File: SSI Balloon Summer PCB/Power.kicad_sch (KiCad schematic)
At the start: 37 parts, among them J1 Battery connector, J2 Raspberry Pi Connector, Q2 DMG2305UX-7, SW1 SW_SPDT, U2 TPS63070RNMR, U3 AP2112K-3.3TRG1, U6 TPS63070RNMR

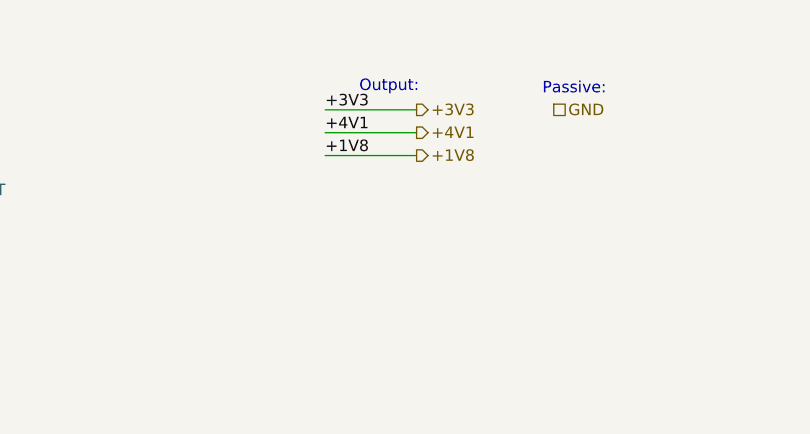
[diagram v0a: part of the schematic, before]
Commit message: Finished sensors + tidied up schematic
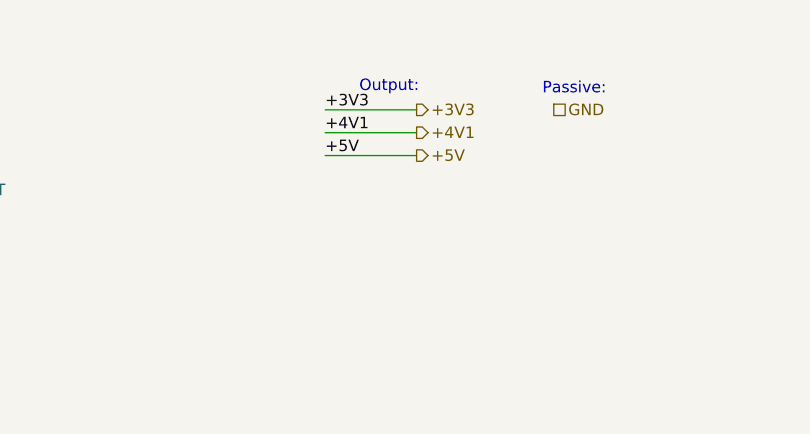
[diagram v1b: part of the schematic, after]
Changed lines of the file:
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@@
+	(wire
+		(pts
+			(xy 226.06 35.56) (xy 236.22 35.56)
+		)
+		(stroke
+			(width 0)
+			(type default)
+		)
+	)
 	(wire
 		(pts
@@
 		(pts
 			(xy 114.3 168.91) (xy 114.3 171.45)
-		)
-		(stroke
-			(width 0)
-			(type default)
-		)
-	)
-	(wire
-		(pts
-			(xy 226.06 35.56) (xy 236.22 35.56)
 		)
 		(stroke
@@
 		)
 	)
-	(label "+1V8"
+	(label "+5V"
 		(at 226.06 35.56 0)
 		(effects
@@
 		)
 	)
-	(hierarchical_label "+1V8"
+	(hierarchical_label "+5V"
 		(shape output)
 		(at 236.22 35.56 0)

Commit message: tidying
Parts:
- removed J2: Raspberry Pi Connector, symbol Connector_Generic:Conn_01x02
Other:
- moved on the sheet: C10, C9, U3

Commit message: Minor tweaks, renamed some pins
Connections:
- no-connect marks 0 -> 1
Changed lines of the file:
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@@
 	)
 	(junction
-		(at 97.79 46.99)
+		(at 82.55 46.99)
 		(diameter 0)
 		(color 0 0 0 0)
@@
 	)
 	(junction
+		(at 97.79 46.99)
+		(diameter 0)
+		(color 0 0 0 0)
+	)
+	(junction
 		(at 267.97 119.38)
 		(diameter 0)
@@
 		(color 0 0 0 0)
 	)
+	(no_connect
+		(at 134.62 50.8)
+	)
 	(wire
 		(pts
@@
 	(wire
 		(pts
-			(xy 92.71 46.99) (xy 97.79 46.99)
+			(xy 82.55 46.99) (xy 97.79 46.99)
 		)
 		(stroke
@@
 	(symbol
 		(lib_id "power:VAA")
-		(at 92.71 46.99 0)
+		(at 82.55 46.99 0)
 		(unit 1)
 		(body_style 1)
@@
 		(fields_autoplaced yes)
 		(property "Reference" "#PWR062"
-			(at 92.71 50.8 0)
+			(at 82.55 50.8 0)
 			(hide yes)
 			(show_name no)
@@
 		)
 		(property "Value" "VBAT"
-			(at 92.71 41.91 0)
+			(at 82.55 41.91 0)
 			(show_name no)
 			(do_not_autoplace no)
@@
 		)
 		(property "Footprint" ""
-			(at 92.71 46.99 0)
+			(at 82.55 46.99 0)
 			(hide yes)
 			(show_name no)
@@
 		)
 		(property "Datasheet" ""
-			(at 92.71 46.99 0)
+			(at 82.55 46.99 0)
 			(hide yes)
 			(show_name no)
@@
 		)
 		(property "Description" "Power symbol creates a global label with name \"VBAT\""
-			(at 92.71 46.99 0)
+			(at 82.55 46.99 0)
 			(hide yes)
 			(show_name no)
@@
 					(unit 1)
 				)
+			)
+		)
+	)
+	(symbol
+		(lib_id "power:PWR_FLAG")
+		(at 82.55 46.99 180)
+		(unit 1)
+		(body_style 1)
+		(exclude_from_sim no)
+		(in_bom yes)
+		(on_board yes)
+		(in_pos_files yes)
+		(dnp no)
+		(fields_autoplaced yes)
+		(property "Reference" "#FLG01"
+			(at 82.55 48.895 0)
+			(hide yes)
+			(show_name no)
+			(do_not_autoplace no)
+			(effects
+				(font
+					(size 1.27 1.27)
+				)
+			)
+		)
+		(property "Value" "PWR_FLAG"
+			(at 82.55 52.07 0)
+			(show_name no)
+			(do_not_autoplace no)
+			(effects
+				(font
+					(size 1.27 1.27)
+				)
+			)
+		)
+		(property "Footprint" ""
+			(at 82.55 46.99 0)
+			(hide yes)
+			(show_name no)
+			(do_not_autoplace no)
+			(effects
+				(font
+					(size 1.27 1.27)
+				)
+			)
+		)
+		(property "Datasheet" ""
+			(at 82.55 46.99 0)
+			(hide yes)
+			(show_name no)
+			(do_not_autoplace no)
+			(effects
+				(font
+					(size 1.27 1.27)
+				)
+			)
+		)
+		(property "Description" "Special symbol for telling ERC where power comes from"
+			(at 82.55 46.99 0)
+			(hide yes)
+			(show_name no)
+			(do_not_autoplace no)
+			(effects
+				(font
+					(size 1.27 1.27)
+				)
+			)
+		)
+		(pin "1"
+		)
+		(instances
+			(project "SSI Summer Balloons"
+				(path "/3c45a535-6e6b-4825-ad52-82c10cbe7866/1b5737e2-4399-496a-b942-ad94430e2078"
+					(reference "#FLG01")
+					(unit 1)
+				)

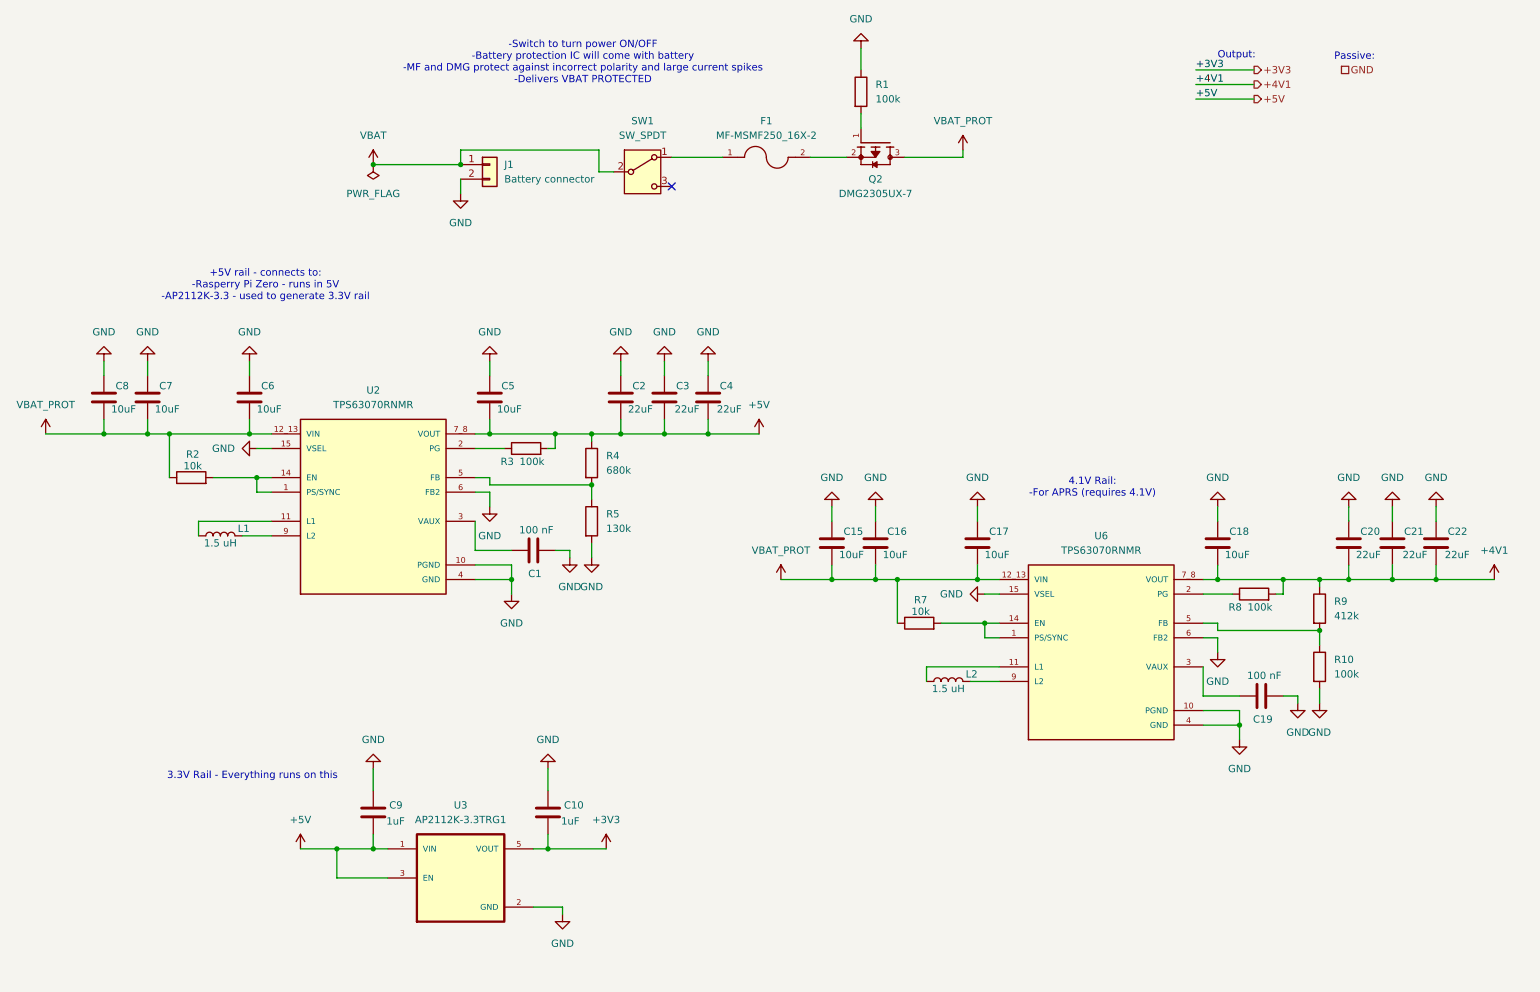
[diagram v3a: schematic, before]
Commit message: Fixed ERC - no ERC errors
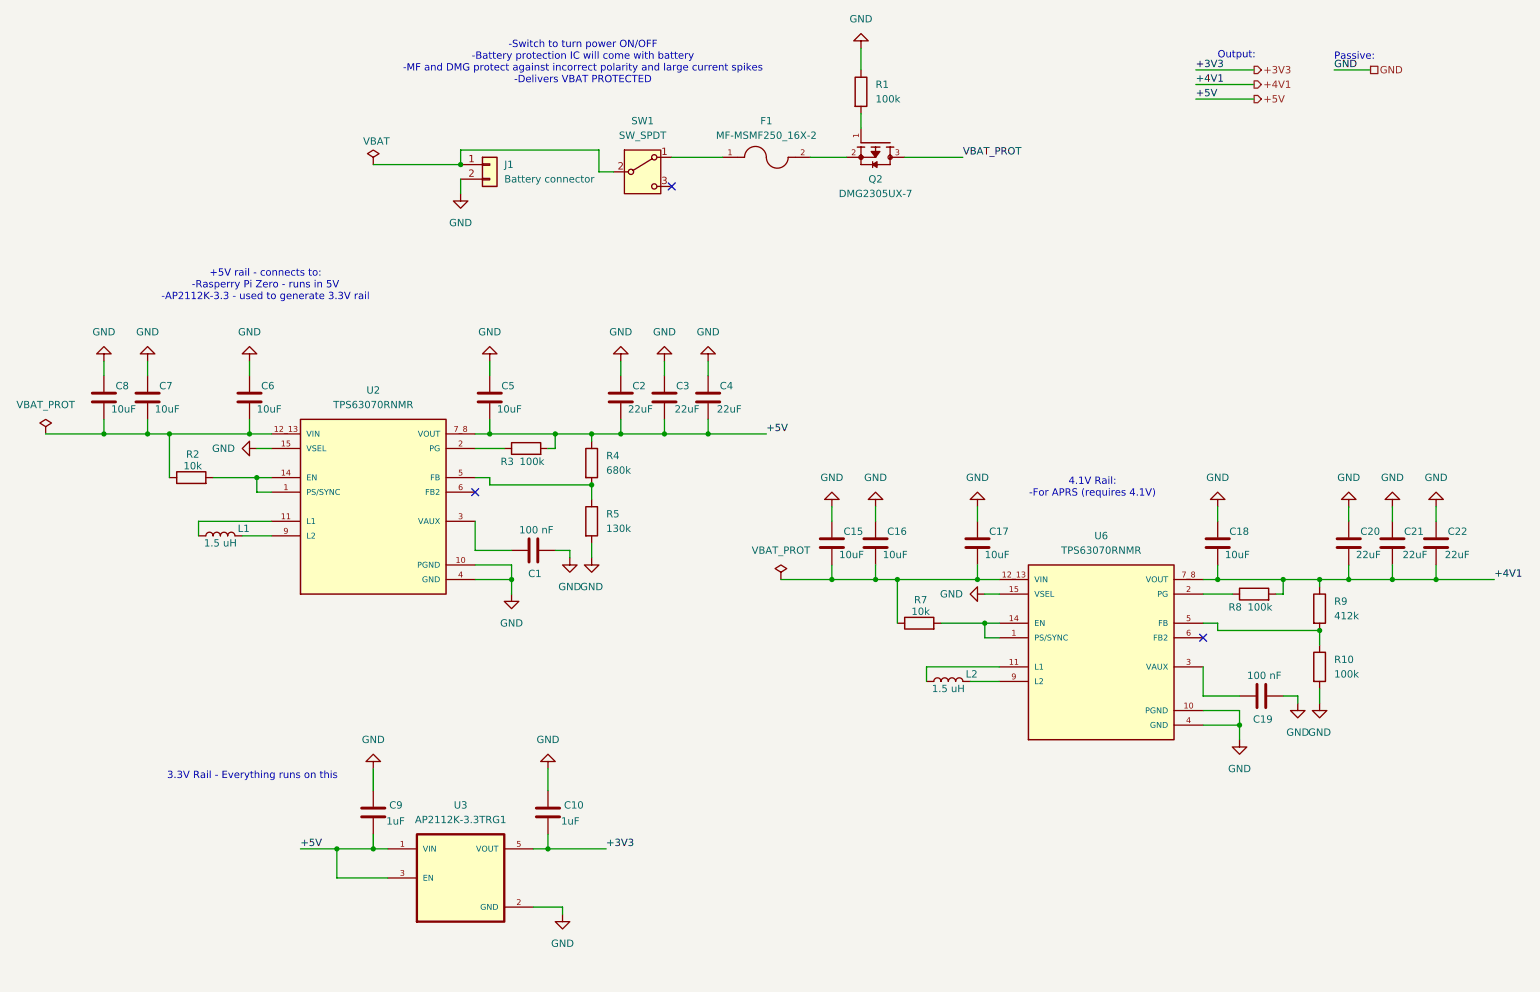
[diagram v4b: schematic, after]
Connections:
- net GND: no longer U2.6 (FB2), U6.6 (FB2)
- net VBAT_PROT: no longer C15.2, C16.2, C17.2, C6.2, C7.2, C8.2, R2.1, R7.1, U2.12_13 (VIN), U6.12_13 (VIN)
- net VBAT: no longer names the net of J1.1 (Pin_1), SW1.2 (B)
- new net: C6.2, C7.2, C8.2, R2.1, U2.12_13 (VIN)
- new net: C15.2, C16.2, C17.2, R7.1, U6.12_13 (VIN)
- no-connect marks 1 -> 3
